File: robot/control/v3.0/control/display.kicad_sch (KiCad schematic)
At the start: 3 parts, among them J14 Conn_02x05_Odd_Even, Q4 BSS138K

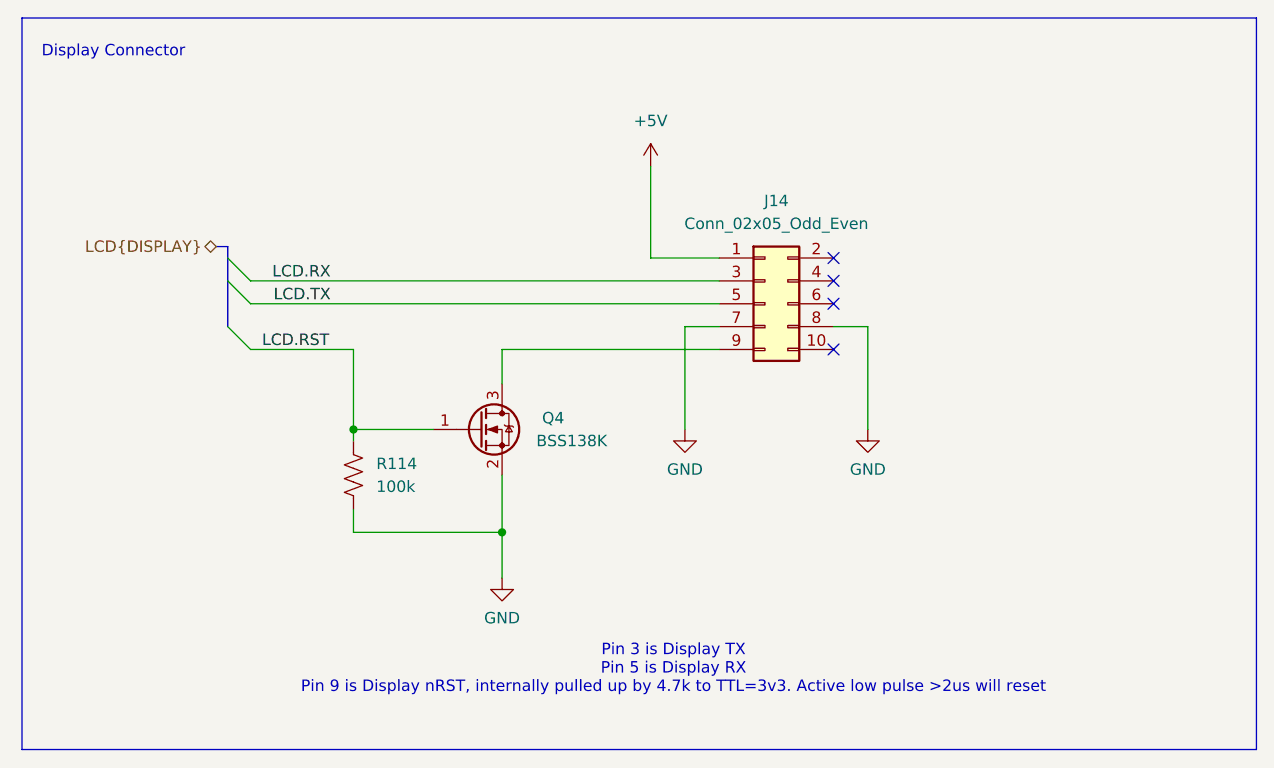
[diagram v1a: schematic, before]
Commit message: update boot mode docs, schematic visual fixes, UART default state fixes
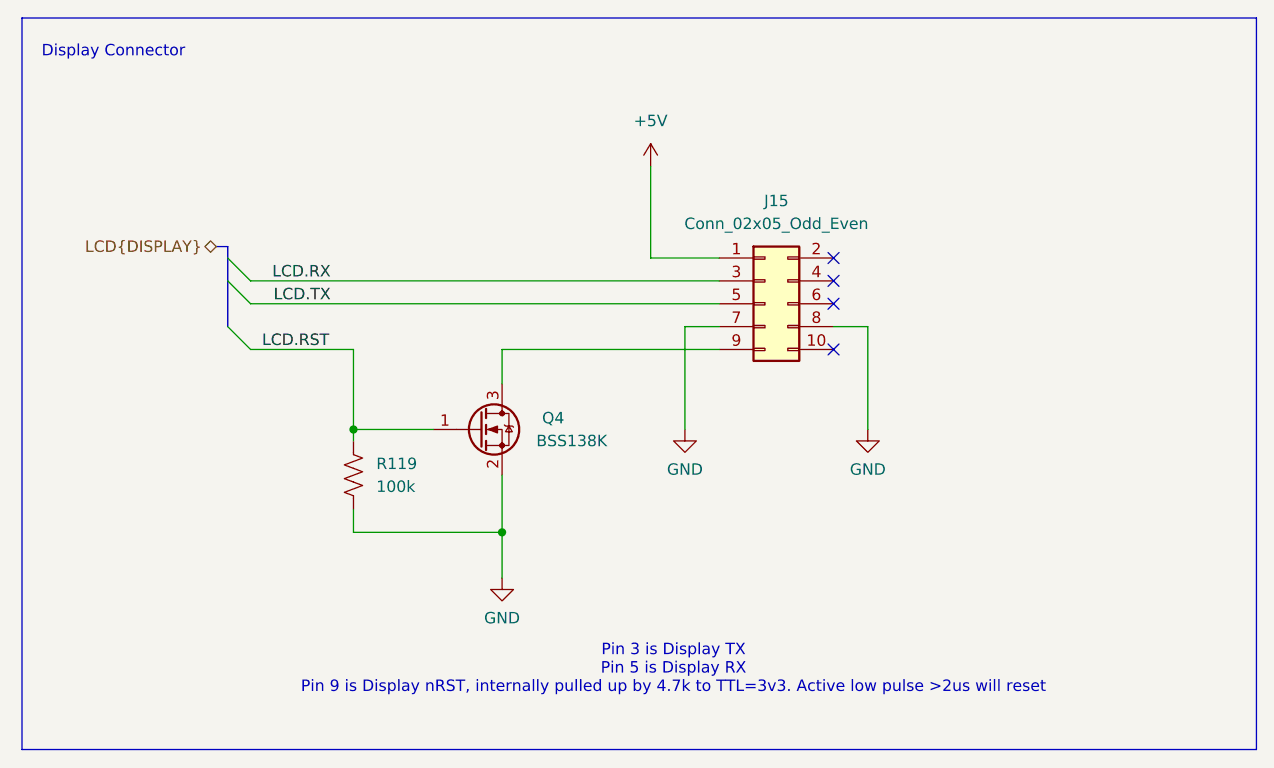
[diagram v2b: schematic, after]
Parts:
- renumbered J14 to J15, R114 to R119
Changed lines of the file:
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@@
 	(label "LCD.TX"
 		(at 55.88 52.07 180)
+		(fields_autoplaced yes)
 		(effects
 			(font
@@
 	(label "LCD.RX"
 		(at 55.88 49.53 180)
+		(fields_autoplaced yes)
 		(effects
 			(font
@@
 	(label "LCD.RST"
 		(at 48.26 57.15 0)
+		(fields_autoplaced yes)
 		(effects
 			(font
@@
 		(dnp no)
 		(fields_autoplaced yes)
-		(property "Reference" "#PWR0185"
+		(property "Reference" "#PWR0191"
 			(at 91.44 40.64 0)
 			(effects
@@
 			(project ""
 				(path "/847d0bbe-37dc-4895-9fde-3757dcb8f4e8/75097bdf-0d28-4d38-a3d8-764c6ca96c04"
-					(reference "#PWR0185")
+					(reference "#PWR0191")
 					(unit 1)
 				)
@@
 		(dnp no)
 		(fields_autoplaced yes)
-		(property "Reference" "#PWR0186"
+		(property "Reference" "#PWR0192"
 			(at 95.25 72.39 0)
 			(effects
@@
 			(project "control"
 				(path "/847d0bbe-37dc-4895-9fde-3757dcb8f4e8/75097bdf-0d28-4d38-a3d8-764c6ca96c04"
-					(reference "#PWR0186")
+					(reference "#PWR0192")
 					(unit 1)
 				)
@@
 		(dnp no)
 		(fields_autoplaced yes)
-		(property "Reference" "#PWR0187"
+		(property "Reference" "#PWR0193"
 			(at 115.57 72.39 0)
 			(effects
@@
 			(project "control"
 				(path "/847d0bbe-37dc-4895-9fde-3757dcb8f4e8/75097bdf-0d28-4d38-a3d8-764c6ca96c04"
-					(reference "#PWR0187")
+					(reference "#PWR0193")
 					(unit 1)
 				)
@@
 		(dnp no)
 		(fields_autoplaced yes)
-		(property "Reference" "#PWR0188"
+		(property "Reference" "#PWR0194"
 			(at 74.93 88.9 0)
 			(effects
@@
 			(project "control"
 				(path "/847d0bbe-37dc-4895-9fde-3757dcb8f4e8/75097bdf-0d28-4d38-a3d8-764c6ca96c04"
-					(reference "#PWR0188")
+					(reference "#PWR0194")
 					(unit 1)
 				)
@@
 		(dnp no)
 		(fields_autoplaced yes)
-		(property "Reference" "R114"
+		(property "Reference" "R119"
 			(at 60.96 69.8499 0)
 			(effects
@@
 			(project "control"
 				(path "/847d0bbe-37dc-4895-9fde-3757dcb8f4e8/75097bdf-0d28-4d38-a3d8-764c6ca96c04"
-					(reference "R114")
+					(reference "R119")
 					(unit 1)
 				)
@@
 		(dnp no)
 		(fields_autoplaced yes)
-		(property "Reference" "J14"
+		(property "Reference" "J15"
 			(at 105.41 40.64 0)
 			(effects
@@
 			(project ""
 				(path "/847d0bbe-37dc-4895-9fde-3757dcb8f4e8/75097bdf-0d28-4d38-a3d8-764c6ca96c04"
-					(reference "J14")
-					(unit 1)
-				)
+					(reference "J15")
+					(unit 1)
+				)

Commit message: footprint selection done, placement work
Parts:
- J15: footprint (none) -> Connector_PinHeader_2.54mm:PinHeader_2x05_P2.54mm_Vertical
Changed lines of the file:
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@@
 			)
 		)
-		(property "Footprint" ""
+		(property "Footprint" "Connector_PinHeader_2.54mm:PinHeader_2x05_P2.54mm_Vertical"
 			(at 104.14 52.07 0)
 			(effects

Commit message: initial coase placement done
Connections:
- net +5V: now also J15.9 (Pin_9); no longer J15.1 (Pin_1)
- net GND: now also J15.3 (Pin_3), J15.4 (Pin_4); no longer J15.7 (Pin_7), J15.8 (Pin_8)
- net LCD.RX: now also J15.7 (Pin_7); no longer J15.3 (Pin_3)
- net at Q4.3 (D): now also J15.1 (Pin_1); no longer J15.9 (Pin_9)
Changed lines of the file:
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@@
 		(lib_id "Connector_Generic:Conn_02x05_Odd_Even")
 		(at 104.14 52.07 0)
+		(mirror x)
 		(unit 1)
 		(exclude_from_sim no)
@@
 		(on_board yes)
 		(dnp no)
-		(fields_autoplaced yes)
 		(property "Reference" "J15"
-			(at 105.41 40.64 0)
+			(at 105.41 43.18 0)
 			(effects
 				(font
@@
 		)
 		(property "Value" "Conn_02x05_Odd_Even"
-			(at 105.41 43.18 0)
+			(at 105.41 40.64 0)
 			(effects
 				(font
